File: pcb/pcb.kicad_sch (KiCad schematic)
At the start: 27 parts, among them J1 Screw_Terminal_01x02, J2 Screw_Terminal_01x04, J3 Screw_Terminal_01x04, J5 Screw_Terminal_01x06, J6 Screw_Terminal_01x04, Q1 2N7000, Q2 2N7000, Q3 2N7000

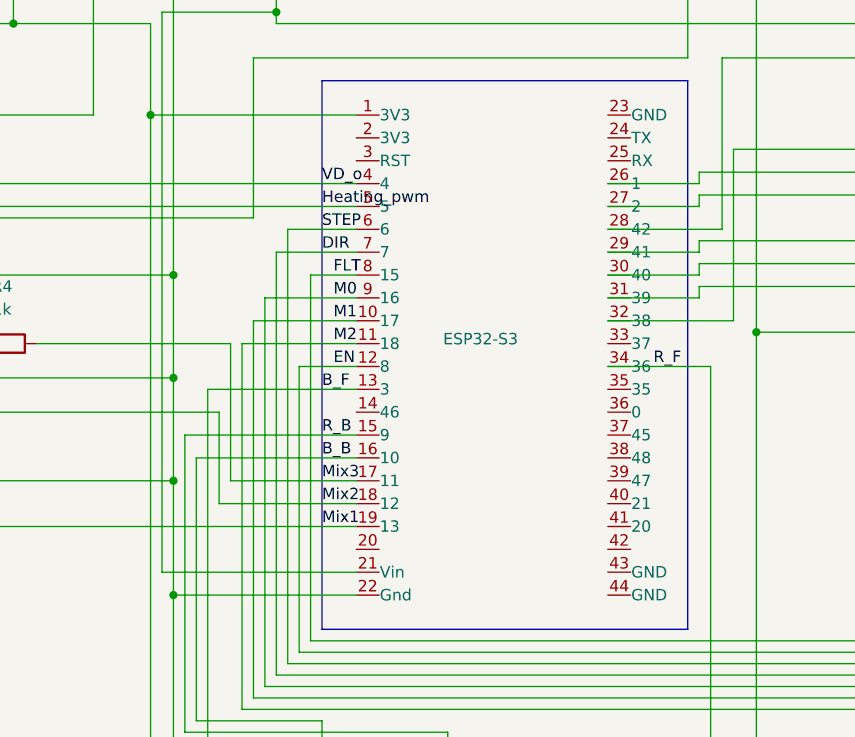
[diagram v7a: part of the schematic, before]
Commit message: finished labeling esp connections
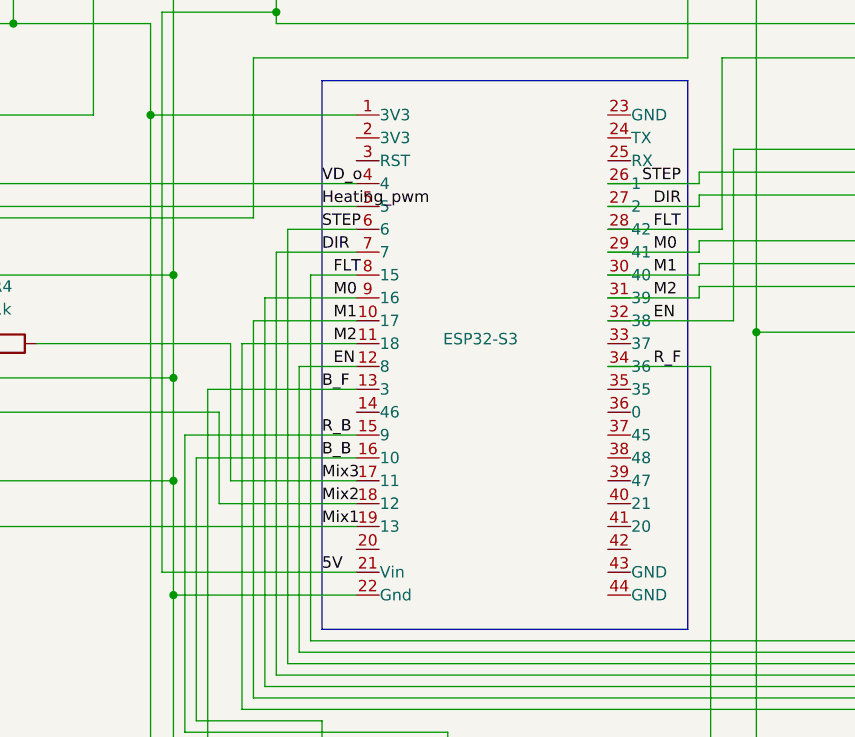
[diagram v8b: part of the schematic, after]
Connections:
- net DIR: now also A1.16 (DIR), ESP32-S3.27 (2)
- net EN: now also A1.9 (~{EN}), ESP32-S3.32 (38)
- net FLT: now also A1.2 (~{FLT}), ESP32-S3.28 (42)
- net M0: now also A1.10 (M0), ESP32-S3.29 (41)
- net M1: now also A1.11 (M1), ESP32-S3.30 (40)
- net M2: now also A1.12 (M2), ESP32-S3.31 (39)
- net STEP: now also A1.15 (STEP), ESP32-S3.26 (1)
- net 5V: now reaches A1.13 (~{RST}), A1.14 (~{SLP}), A2.13 (~{RST}), A2.14 (~{SLP}), ESP32-S3.21 (Vin), OutputCap1.2, Regulator1.2 (VO)
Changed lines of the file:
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@@
-	(wire
-		(pts
-			(xy 144.78 106.68) (xy 123.19 106.68)
-		)
-		(stroke
-			(width 0)
-			(type default)
-		)
-	)
 	(wire
 		(pts
@@
 	(wire
 		(pts
+			(xy 123.19 106.68) (xy 144.78 106.68)
+		)
+		(stroke
+			(width 0)
+			(type default)
+		)
+	)
+	(wire
+		(pts
 			(xy 124.46 24.13) (xy 129.54 24.13)
 		)
@@
 			(width 0)
 			(type default)
+		)
+	)
+	(label "M2"
+		(at 177.8 76.2 0)
+		(effects
+			(font
+				(size 1.27 1.27)
+			)
+			(justify left bottom)
+		)
+	)
+	(label "M0"
+		(at 177.8 71.12 0)
+		(effects
+			(font
+				(size 1.27 1.27)
+			)
+			(justify left bottom)
 		)
 	)
@@
 		)
 	)
+	(label "STEP"
+		(at 176.53 63.5 0)
+		(effects
+			(font
+				(size 1.27 1.27)
+			)
+			(justify left bottom)
+		)
+	)
 	(label "Mix1"
 		(at 140.97 101.6 0)
@@
 		)
 	)
+	(label "5V"
+		(at 140.97 106.68 0)
+		(effects
+			(font
+				(size 1.27 1.27)
+			)
+			(justify left bottom)
+		)
+	)
+	(label "DIR"
+		(at 177.8 66.04 0)
+		(effects
+			(font
+				(size 1.27 1.27)
+			)
+			(justify left bottom)
+		)
+	)
 	(label "VD_o"
 		(at 140.97 63.5 0)
@@
 	)
 	(label "FLT"
+		(at 177.8 68.58 0)
+		(effects
+			(font
+				(size 1.27 1.27)
+			)
+			(justify left bottom)
+		)
+	)
+	(label "EN"
+		(at 177.8 78.74 0)
+		(effects
+			(font
+				(size 1.27 1.27)
+			)
+			(justify left bottom)
+		)
+	)
+	(label "FLT"
 		(at 142.24 73.66 0)
 		(effects
 			(font
+				(size 1.27 1.27)
+			)
+			(justify left bottom)
+		)
+	)
+	(label "M1"
+		(at 177.8 73.66 0)
+		(effects
+			(font
